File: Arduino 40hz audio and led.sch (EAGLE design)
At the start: 38 parts, among them IC1 LM7805, IC2 IRL-Z44N, IC3 LM741

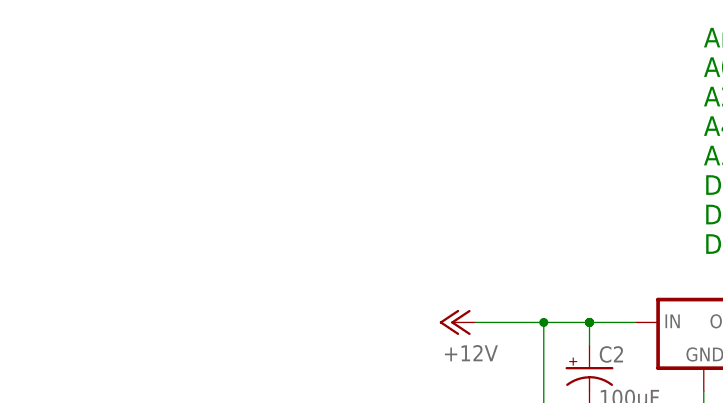
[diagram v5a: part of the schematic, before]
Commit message: Minor updates
Minor updates, mainly to texted in the schematic.
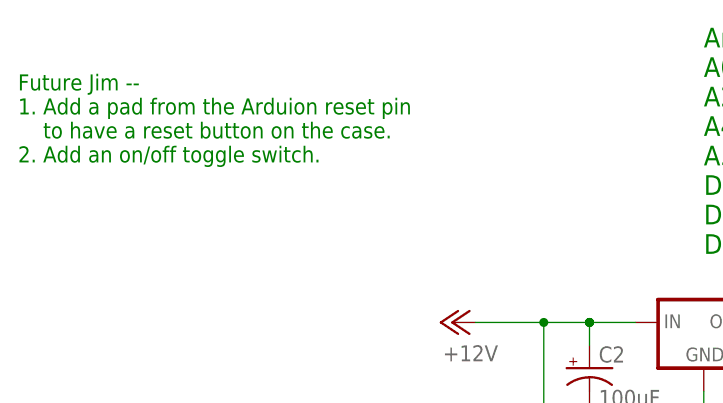
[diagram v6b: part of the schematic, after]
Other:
- note added: "Future Jim -- 1. Add a pad from the Arduion reset pin to have a reset button on the case. 2. Add an on/off toggle switch."
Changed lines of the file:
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@@
 <grid distance="0.1" unitdist="inch" unit="inch" style="lines" multiple="1" display="no" altdistance="0.01" altunitdist="inch" altunit="inch"/>
 <layers>
-<layer number="1" name="Top" color="4" fill="1" visible="yes" active="no"/>
-<layer number="2" name="Route2" color="16" fill="1" visible="yes" active="no"/>
-<layer number="3" name="Route3" color="17" fill="1" visible="yes" active="no"/>
-<layer number="4" name="Route4" color="18" fill="1" visible="yes" active="no"/>
-<layer number="5" name="Route5" color="19" fill="1" visible="yes" active="no"/>
-<layer number="6" name="Route6" color="25" fill="1" visible="yes" active="no"/>
-<layer number="7" name="Route7" color="26" fill="1" visible="yes" active="no"/>
-<layer number="8" name="Route8" color="27" fill="1" visible="yes" active="no"/>
-<layer number="9" name="Route9" color="28" fill="1" visible="yes" active="no"/>
-<layer number="10" name="Route10" color="29" fill="1" visible="yes" active="no"/>
-<layer number="11" name="Route11" color="30" fill="1" visible="yes" active="no"/>
-<layer number="12" name="Route12" color="20" fill="1" visible="yes" active="no"/>
-<layer number="13" name="Route13" color="21" fill="1" visible="yes" active="no"/>
-<layer number="14" name="Route14" color="22" fill="1" visible="yes" active="no"/>
-<layer number="15" name="Route15" color="23" fill="1" visible="yes" active="no"/>
-<layer number="16" name="Bottom" color="1" fill="1" visible="yes" active="no"/>
-<layer number="17" name="Pads" color="2" fill="1" visible="yes" active="no"/>
-<layer number="18" name="Vias" color="2" fill="1" visible="yes" active="no"/>
-<layer number="19" name="Unrouted" color="6" fill="1" visible="yes" active="no"/>
-<layer number="20" name="Dimension" color="24" fill="1" visible="yes" active="no"/>
-<layer number="21" name="tPlace" color="7" fill="1" visible="yes" active="no"/>
-<layer number="22" name="bPlace" color="7" fill="1" visible="yes" active="no"/>
-<layer number="23" name="tOrigins" color="15" fill="1" visible="yes" active="no"/>
-<layer number="24" name="bOrigins" color="15" fill="1" visible="yes" active="no"/>
-<layer number="25" name="tNames" color="7" fill="1" visible="yes" active="no"/>
-<layer number="26" name="bNames" color="7" fill="1" visible="yes" active="no"/>
-<layer number="27" name="tValues" color="7" fill="1" visible="yes" active="no"/>
-<layer number="28" name="bValues" color="7" fill="1" visible="yes" active="no"/>
+<layer number="1" name="Top" color="4" fill="1" visible="no" active="no"/>
+<layer number="2" name="Route2" color="16" fill="1" visible="no" active="no"/>
+<layer number="3" name="Route3" color="17" fill="1" visible="no" active="no"/>
+<layer number="4" name="Route4" color="18" fill="1" visible="no" active="no"/>
+<layer number="5" name="Route5" color="19" fill="1" visible="no" active="no"/>
+<layer number="6" name="Route6" color="25" fill="1" visible="no" active="no"/>
+<layer number="7" name="Route7" color="26" fill="1" visible="no" active="no"/>
+<layer number="8" name="Route8" color="27" fill="1" visible="no" active="no"/>
+<layer number="9" name="Route9" color="28" fill="1" visible="no" active="no"/>
+<layer number="10" name="Route10" color="29" fill="1" visible="no" active="no"/>
+<layer number="11" name="Route11" color="30" fill="1" visible="no" active="no"/>
+<layer number="12" name="Route12" color="20" fill="1" visible="no" active="no"/>
+<layer number="13" name="Route13" color="21" fill="1" visible="no" active="no"/>
+<layer number="14" name="Route14" color="22" fill="1" visible="no" active="no"/>
+<layer number="15" name="Route15" color="23" fill="1" visible="no" active="no"/>
+<layer number="16" name="Bottom" color="1" fill="1" visible="no" active="no"/>
+<layer number="17" name="Pads" color="2" fill="1" visible="no" active="no"/>
+<layer number="18" name="Vias" color="2" fill="1" visible="no" active="no"/>
+<layer number="19" name="Unrouted" color="6" fill="1" visible="no" active="no"/>
+<layer number="20" name="Dimension" color="24" fill="1" visible="no" active="no"/>
+<layer number="21" name="tPlace" color="7" fill="1" visible="no" active="no"/>
+<layer number="22" name="bPlace" color="7" fill="1" visible="no" active="no"/>
+<layer number="23" name="tOrigins" color="15" fill="1" visible="no" active="no"/>
+<layer number="24" name="bOrigins" color="15" fill="1" visible="no" active="no"/>
+<layer number="25" name="tNames" color="7" fill="1" visible="no" active="no"/>
+<layer number="26" name="bNames" color="7" fill="1" visible="no" active="no"/>
+<layer number="27" name="tValues" color="7" fill="1" visible="no" active="no"/>
+<layer number="28" name="bValues" color="7" fill="1" visible="no" active="no"/>
 <layer number="29" name="tStop" color="7" fill="3" visible="no" active="no"/>
 <layer number="30" name="bStop" color="7" fill="6" visible="no" active="no"/>
@@
 <layer number="35" name="tGlue" color="7" fill="4" visible="no" active="no"/>
 <layer number="36" name="bGlue" color="7" fill="5" visible="no" active="no"/>
-<layer number="37" name="tTest" color="7" fill="1" visible="yes" active="no"/>
-<layer number="38" name="bTest" color="7" fill="1" visible="yes" active="no"/>
+<layer number="37" name="tTest" color="7" fill="1" visible="no" active="no"/>
+<layer number="38" name="bTest" color="7" fill="1" visible="no" active="no"/>
 <layer number="39" name="tKeepout" color="4" fill="11" visible="no" active="no"/>
 <layer number="40" name="bKeepout" color="1" fill="11" visible="no" active="no"/>
@@
 <layer number="44" name="Drills" color="7" fill="1" visible="no" active="no"/>
 <layer number="45" name="Holes" color="7" fill="1" visible="no" active="no"/>
-<layer number="46" name="Milling" color="3" fill="1" visible="yes" active="no"/>
-<layer number="47" name="Measures" color="7" fill="1" visible="yes" active="no"/>
-<layer number="48" name="Document" color="7" fill="1" visible="yes" active="no"/>
-<layer number="49" name="Reference" color="7" fill="1" visible="yes" active="no"/>
-<layer number="50" name="dxf" color="7" fill="1" visible="yes" active="no"/>
-<layer number="51" name="tDocu" color="7" fill="1" visible="yes" active="no"/>
-<layer number="52" name="bDocu" color="7" fill="1" visible="yes" active="no"/>
-<layer number="53" name="tGND_GNDA" color="7" fill="9" visible="yes" active="no"/>
-<layer number="54" name="bGND_GNDA" color="1" fill="9" visible="yes" active="no"/>
-<layer number="56" name="wert" color="7" fill="1" visible="yes" active="no"/>
-<layer number="57" name="tCAD" color="7" fill="1" visible="yes" active="no"/>
-<layer number="59" name="tCarbon" color="7" fill="1" visible="yes" active="no"/>
-<layer number="60" name="bCarbon" color="7" fill="1" visible="yes" active="no"/>
+<layer number="46" name="Milling" color="3" fill="1" visible="no" active="no"/>
+<layer number="47" name="Measures" color="7" fill="1" visible="no" active="no"/>
+<layer number="48" name="Document" color="7" fill="1" visible="no" active="no"/>
+<layer number="49" name="Reference" color="7" fill="1" visible="no" active="no"/>
+<layer number="50" name="dxf" color="7" fill="1" visible="no" active="no"/>
+<layer number="51" name="tDocu" color="7" fill="1" visible="no" active="no"/>
+<layer number="52" name="bDocu" color="7" fill="1" visible="no" active="no"/>
+<layer number="53" name="tGND_GNDA" color="7" fill="9" visible="no" active="no"/>
+<layer number="54" name="bGND_GNDA" color="1" fill="9" visible="no" active="no"/>
+<layer number="56" name="wert" color="7" fill="1" visible="no" active="no"/>
+<layer number="57" name="tCAD" color="7" fill="1" visible="no" active="no"/>
+<layer number="59" name="tCarbon" color="7" fill="1" visible="no" active="no"/>
+<layer number="60" name="bCarbon" color="7" fill="1" visible="no" active="no"/>
 <layer number="88" name="SimResults" color="9" fill="1" visible="yes" active="yes"/>
 <layer number="89" name="SimProbes" color="9" fill="1" visible="yes" active="yes"/>
@@
 <text x="40.64" y="45.72" size="1.778" layer="91" rot="R90">LCD SDA</text>
 <text x="40.64" y="30.48" size="1.778" layer="91" rot="R90">LCD SCL</text>
+<text x="-38.1" y="114.3" size="1.778" layer="91">Future Jim --
+1. Add a pad from the Arduion reset pin
+    to have a reset button on the case.
+2. Add an on/off toggle switch.</text>
 </plain>
 <instances>
